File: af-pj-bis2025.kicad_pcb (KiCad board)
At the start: 2 copper layers, 70 x 88.8 mm, 101 parts, among them J1 Barrel_Jack_MountingPin, J10 Conn_01x02, J11 Conn_01x02, J2 CN7, J3 Conn_Coaxial, J4 Conn_Coaxial, J5 CN10, J6 Conn_01x10, J7 Conn_01x06, J8 Conn_01x02, J9 Conn_01x02, U1 MIC5237-5.0YU, U2 ALD114904APAL, U3 OPA2380AIDGKR, U4 THS4552IPWR, U5 REF5050IDR, U6 LT1991ACMS-TRPBF, U7 UA78L06ACPK, U8 ADS1220IPW

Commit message: initial commit
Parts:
- added D1: LED, LED_SMD:LED_0805_2012Metric_Pad1.15x1.40mm_HandSolder, F.Cu at (169.5, 70.0)
- added J12: FH28-10S-0.5SH_05_, pj-bis2025:HIROSE_FH28-10S-0.5SH_05_, F.Cu at (203.0, 139.0)
- added R32: 47, Resistor_SMD:R_0805_2012Metric_Pad1.20x1.40mm_HandSolder, F.Cu at (192.5, 130.0)
- added R33: 47, Resistor_SMD:R_0805_2012Metric_Pad1.20x1.40mm_HandSolder, F.Cu at (195.0, 130.0)
- added R34: 47, Resistor_SMD:R_0805_2012Metric_Pad1.20x1.40mm_HandSolder, F.Cu at (197.5, 130.0)
- added R35: 47, Resistor_SMD:R_0805_2012Metric_Pad1.20x1.40mm_HandSolder, F.Cu at (200.0, 130.0)
- added R36: 698, Resistor_SMD:R_0805_2012Metric_Pad1.20x1.40mm_HandSolder, F.Cu at (174.0, 70.0)
- added R37: 10k, Resistor_SMD:R_0805_2012Metric_Pad1.20x1.40mm_HandSolder, F.Cu at (168.5, 132.0)
- added SW1: PTS 647 SN50 SMTR2 LFS, pj-bis2025:PTS_647_SN50_SMTR2_LFS_PTS 647 SN50 SMTR2 LFS-M, F.Cu at (155.0, 76.5)
- added SW2: PTS 647 SN50 SMTR2 LFS, pj-bis2025:PTS_647_SN50_SMTR2_LFS_PTS 647 SN50 SMTR2 LFS-M, F.Cu at (161.0, 133.5)
- C1: footprint pj-bis2025:LDO_5V_out_TAJR105K016RNJAC_TAJR_AVX -> Capacitor_SMD:C_0805_2012Metric_Pad1.18x1.45mm_HandSolder
- C11, C9: value 3.18n -> 47n
- C12, C7: value 0.1u -> 47n
- C20, C6, C8: value 0.1u -> 0.1u_pass
- C4, C5: value 3.18n -> 4.7n
- R3, R4: value 50k -> 2.4k
- U1: value MIC5237-5.0YU -> MIC5237-5.0YT; footprint pj-bis2025:MIC5237-TO-263-3_MCL-M -> pj-bis2025:MIC5237_5_0YT
- moved J6 9.00 mm to (170.8, 139.0)
- moved TP10 8.49 mm to (159.5, 140.0)
- moved TP11 8.49 mm to (164.0, 140.0)
- moved TP8 8.49 mm to (150.5, 140.0)
- moved TP9 8.49 mm to (155.0, 140.0)
- moved U1 7.71 mm to (169.9, 78.0)
- moved C6 6.71 mm to (174.5, 128.8)
- moved C8 6.25 mm to (182.5, 128.8)
- moved TP5 1.80 mm to (150.0, 83.5)
- moved TP14 1.00 mm to (157.0, 83.5)
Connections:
- J2 pad 23: unconnected-(J2-Pin_23-Pad23) -> Net-(J2-Pin_23)
- J6 pad 10: /LCD_SCLK -> Net-(J6-Pin_10)
- J6 pad 7: /LCD_EXTCOMIN -> Net-(J6-Pin_7)
- J6 pad 8: /LCD_CS -> Net-(J6-Pin_8)
- J6 pad 9: /LCD_MOSI -> Net-(J6-Pin_9)
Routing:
- net GND: track 167.2 -> 225.0 mm, vias 3 -> 5
- net +3V3: track 83.6 -> 133.9 mm, vias 0 -> 2
- net /~{RST}: track 0.00 -> 35.6 mm, vias 0 -> 1
- net Net-(J6-Pin_8): track 0.00 -> 32.2 mm, vias 0 -> 2
- net Net-(J2-Pin_23): track 0.00 -> 30.0 mm
- net Net-(J6-Pin_7): track 0.00 -> 27.3 mm, vias 0 -> 2
- net Net-(J6-Pin_9): track 0.00 -> 27.3 mm, vias 0 -> 1
- net Net-(J6-Pin_10): track 0.00 -> 25.1 mm, vias 0 -> 1
- net /LCD_DISP: track 29.4 -> 44.1 mm, vias 0 -> 1
- net /DC_9V: track 41.1 -> 50.6 mm
- net /ADC_DRDY: track 62.0 -> 53.6 mm, vias 2 -> 1
- net /LCD_EXTCOMIN: track 29.5 -> 21.8 mm, vias 0 -> 1
- net /LCD_CS: track 40.5 -> 33.7 mm, vias 1 -> 0
- net /ADC_SCLK: track 66.3 -> 72.7 mm
- net /LCD_SCLK: track 38.7 -> 34.0 mm
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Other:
- board size 70 x 88.8 mm -> 70 x 93.2 mm
- board text added: "2026 Yusuke Akagi"
- board text removed: "2025 Yusuke Akagi"

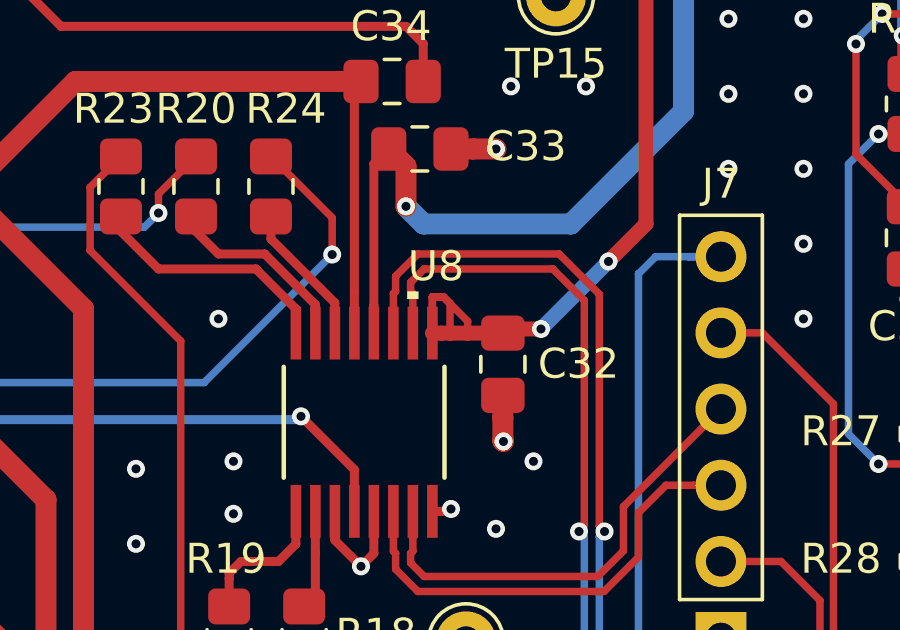
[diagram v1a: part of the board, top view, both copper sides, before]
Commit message: change PCB layout
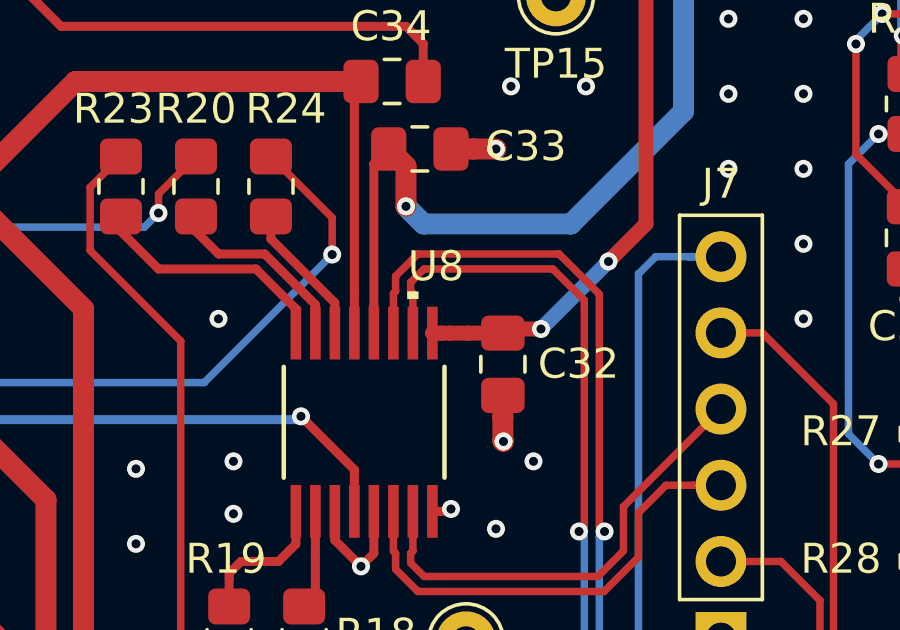
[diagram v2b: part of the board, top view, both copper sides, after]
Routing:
- net /VREF_5V: track 53.0 -> 47.0 mm
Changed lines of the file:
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@@
-	)
-	(segment
-		(start 168.468 109.738)
-		(end 168.247 109.518)
-		(width 0.25)
-		(layer "F.Cu")
-		(net 14)
 	)
 	(segment
@@
 		(end 171.397 88.816)
 		(width 0.5)
-		(layer "F.Cu")
-		(net 14)
-	)
-	(segment
-		(start 169.055 110.326)
-		(end 169.055 110.726)
-		(width 0.25)
 		(layer "F.Cu")
 		(net 14)
@@
 	)
 	(segment
-		(start 167.88 110.726)
-		(end 167.88 109.518)
-		(width 0.25)
-		(layer "F.Cu")
-		(net 14)
-	)
-	(segment
 		(start 170.2304 110.7261)
 		(end 170.2302 110.7259)
@@
 		(end 173.75 108.338)
 		(width 0.5)
-		(layer "F.Cu")
-		(net 14)
-	)
-	(segment
-		(start 168.468 110.726)
-		(end 168.468 109.738)
-		(width 0.25)
 		(layer "F.Cu")
 		(net 14)
@@
 	)
 	(segment
-		(start 167.88 110.726)
-		(end 167.88 109.518)
-		(width 0.25)
-		(layer "F.Cu")
-		(net 14)
-	)
-	(segment
 		(start 175 89.6819)
 		(end 175 91.1509)
@@
 	)
 	(segment
-		(start 167.88 109.518)
-		(end 168.248 109.518)
-		(width 0.25)
-		(layer "F.Cu")
-		(net 14)
-	)
-	(segment
-		(start 167.8805 110.726)
-		(end 167.8804 110.7261)
-		(width 0.25)
-		(layer "F.Cu")
-		(net 14)
-	)
-	(segment
 		(start 172.5 90.128)
 		(end 172.5 89.9185)
-		(width 0.25)
-		(layer "F.Cu")
-		(net 14)
-	)
-	(segment
-		(start 168.248 109.518)
-		(end 169.055 110.326)
 		(width 0.25)
 		(layer "F.Cu")
@@
 		(width 0.25)
 		(layer "F.Cu")
-		(net 14)
-	)
-	(segment
-		(start 168.247 109.518)
-		(end 167.88 109.518)
-		(width 0.25)
-		(layer "F.Cu")

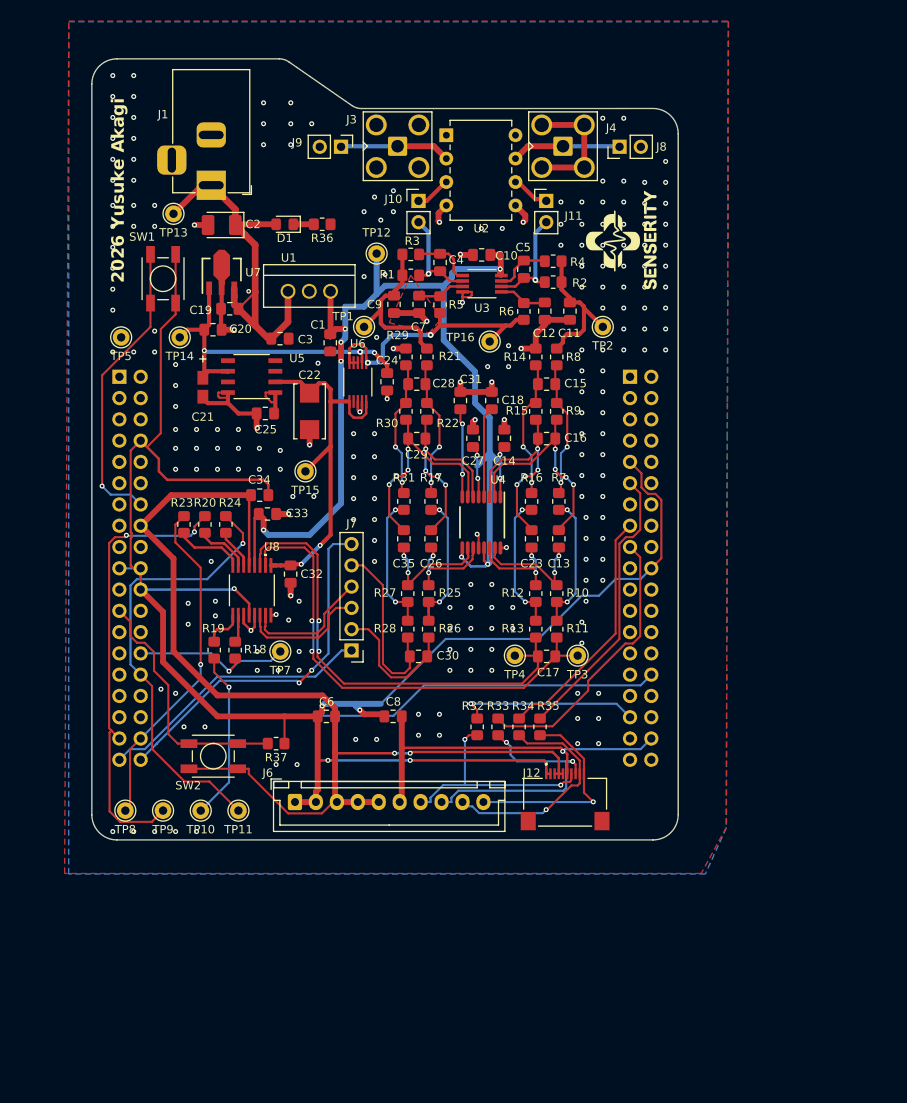
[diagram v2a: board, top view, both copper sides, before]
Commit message: 0.5Vrefのフットプリントを更新
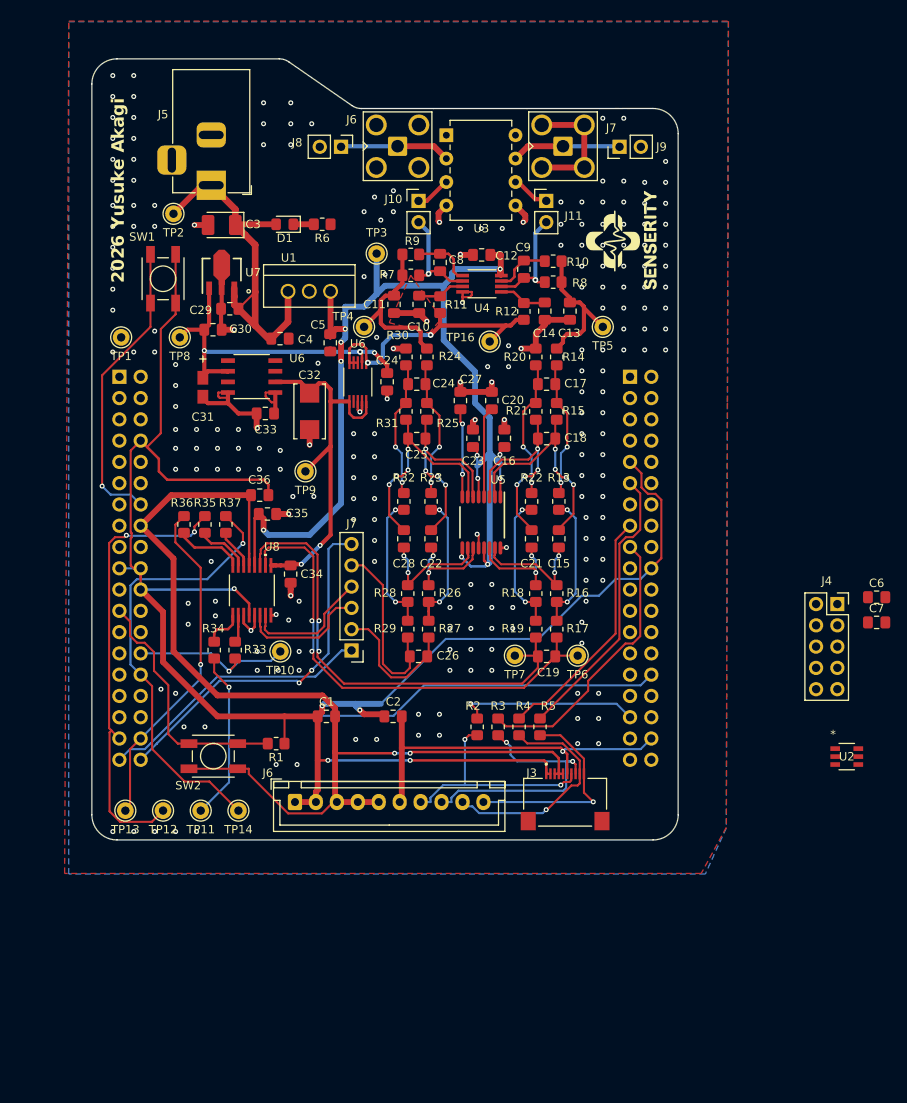
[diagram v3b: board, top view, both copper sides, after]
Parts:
- added C6: 0.1u, Capacitor_SMD:C_0805_2012Metric_Pad1.18x1.45mm_HandSolder, F.Cu at (240.2, 114.5)
- added C7: 0.1u, Capacitor_SMD:C_0805_2012Metric_Pad1.18x1.45mm_HandSolder, F.Cu at (240.2, 117.5)
- added J4: Conn_02x05_Odd_Even, Connector_PinSocket_2.54mm:PinSocket_2x05_P2.54mm_Vertical, F.Cu at (235.5, 115.3)
- added U2: ADR130BUJZ-REEL7, pj-bis2025:ADR130BUJZ_REEL7, F.Cu at (236.6, 133.5)
- renumbered C6 to C1, C7 to C10, C9 to C11, C10 to C12, C11 to C13, C12 to C14, C13 to C15, C14 to C16, C15 to C17, C16 to C18, C17 to C19, C8 to C2, C18 to C20, C23 to C21, C26 to C22, C27 to C23, C28 to C24, C29 to C25, C30 to C26, C31 to C27, C35 to C28, C19 to C29, C2 to C3, C20 to C30, C21 to C31, C22 to C32, C25 to C33, C32 to C34, C33 to C35, C34 to C36, C3 to C4, C1 to C5, C4 to C8, C5 to C9, J2 to J1, J5 to J2, J12 to J3, J1 to J5, J3 to J6, J4 to J7, J9 to J8, J8 to J9, R37 to R1, R4 to R10, R5 to R11, R6 to R12, R7 to R13, R8 to R14, R9 to R15, R10 to R16, R11 to R17, R12 to R18, R13 to R19, R32 to R2, R14 to R20, R15 to R21, R16 to R22, R17 to R23, R21 to R24, R22 to R25, R25 to R26, R26 to R27, R27 to R28, R28 to R29, R33 to R3, R29 to R30, R30 to R31, R31 to R32, R18 to R33, R19 to R34, R20 to R35, R23 to R36, R24 to R37, R34 to R4, R35 to R5, R36 to R6, R1 to R7, R2 to R8, R3 to R9, TP5 to TP1, TP7 to TP10, TP10 to TP11, TP9 to TP12, TP8 to TP13, TP11 to TP14, TP13 to TP2, TP12 to TP3, TP1 to TP4, TP2 to TP5, TP3 to TP6, TP4 to TP7, TP14 to TP8, TP15 to TP9, U2 to U3, U3 to U4, U4 to U5, U5 to U6
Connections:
- C26 pad 1: /AIN2_inP -> /AIN2P
- C26 pad 2: /AIN2_inN -> /AIN2N
- J3 pad 10: Net-(J6-Pin_10) -> Net-(J4-Pin_10)
- J3 pad 7: Net-(J6-Pin_7) -> Net-(J4-Pin_7)
- J3 pad 8: Net-(J6-Pin_8) -> Net-(J4-Pin_8)
- J3 pad 9: Net-(J6-Pin_9) -> Net-(J4-Pin_9)
- R2 pad 2: Net-(J6-Pin_7) -> Net-(J4-Pin_7)
- R27 pad 2: /AIN2_inN -> /AIN2N
- R29 pad 2: /AIN2_inP -> /AIN2P
- R3 pad 2: Net-(J6-Pin_8) -> Net-(J4-Pin_8)
- R4 pad 2: Net-(J6-Pin_9) -> Net-(J4-Pin_9)
- R5 pad 2: Net-(J6-Pin_10) -> Net-(J4-Pin_10)
- U8 pad 6: /AIN2_adcN -> /AIN2N
- U8 pad 7: /AIN2_adcP -> /AIN2P

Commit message: アナログ配線完了
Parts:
- removed the C24 at (181.8, 88.8)
- removed the J6 at (170.8, 139.0)
- removed the J7 at (177.5, 120.9)
- removed the U6 at (178.2, 88.8)
- added TP15: TestPoint, Connector_Pin:Pin_D1.0mm_L10.0mm, F.Cu at (187.0, 124.5)
- added TP16: TestPoint, Connector_Pin:Pin_D1.0mm_L10.0mm, F.Cu at (184.0, 124.5)
- C3: value C_Vin -> 22u
- C4: value 1µF -> 1u
- moved J4 108.1 mm to (141.3, 168.5), turned to 90 degrees
- moved U2 72.2 mm to (179.5, 89.4), turned to 90 degrees
- moved C7 69.1 mm to (178.9, 85.5), turned to 180 degrees
- moved C6 64.0 mm to (180.0, 93.0), turned to 180 degrees
- moved C1 48.0 mm to (142.5, 164.5)
- moved C2 48.0 mm to (150.4, 164.5)
- moved R36 44.7 mm to (189.5, 137.0), turned to 90 degrees
- moved J3 44.2 mm to (171.0, 169.5)
- moved R2 44.2 mm to (160.5, 160.5)
- moved R3 44.2 mm to (163.0, 160.5)
- moved R4 44.2 mm to (165.5, 160.5)
- moved R5 44.2 mm to (168.0, 160.5)
- moved R34 41.5 mm to (200.5, 134.0), turned to 180 degrees
- moved R35 41.2 mm to (187.0, 137.0), turned to -90 degrees
- moved R33 38.5 mm to (200.5, 132.0), turned to 180 degrees
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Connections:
- U8 pad 10: /AIN1N -> /AIN2N
- U8 pad 11: /AIN1P -> /AIN2P
- U8 pad 6: /AIN2N -> /AIN1N
- U8 pad 7: /AIN2P -> /AIN1P
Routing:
- net GND: track 225.0 -> 24.1 mm, vias 5 -> 0
- net +3V3: track 133.9 -> 10.7 mm, vias 2 -> 3
- net /ADC_SCLK: track 72.7 -> 0.00 mm, vias 1 -> 0
- net /ADC_MISO: track 54.2 -> 0.00 mm, vias 2 -> 0
- net /AIN1N: track 59.3 -> 13.5 mm, vias 2 -> 0
- net /AIN1P: track 57.0 -> 11.5 mm, vias 2 -> 0
- net /AIN2_mcuP: track 44.6 -> 0.00 mm, vias 2 -> 0
- net /LCD_DISP: track 44.1 -> 0.00 mm, vias 1 -> 0
- net GNDA: track 89.5 -> 52.2 mm, vias 227 -> 200
- net /LCD_SCLK: track 34.0 -> 0.00 mm
- net /LCD_CS: track 33.7 -> 0.00 mm
- net /AIN2_mcuN: track 33.4 -> 0.00 mm
- net Net-(J6-Pin_8): track 32.2 -> 0.00 mm, vias 2 -> 0
- net Net-(J4-Pin_8): track 0.00 -> 32.2 mm, vias 0 -> 2
- net /ADC_MOSI: track 40.6 -> 9.37 mm, vias 1 -> 0
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
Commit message: GND以外終わり
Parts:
- moved J4 68.8 mm to (161.1, 102.6), turned to 0 degrees
- moved C1 61.9 mm to (155.5, 104.0), turned to 90 degrees
- moved C2 56.3 mm to (155.5, 108.5), turned to -90 degrees
- moved TP11 49.1 mm to (208.5, 137.5)
- moved R2 48.2 mm to (170.1, 113.2), turned to 180 degrees
- moved J3 46.8 mm to (161.1, 123.8), turned to -90 degrees
- moved R3 45.3 mm to (170.1, 115.8), turned to 180 degrees
- moved R4 42.5 mm to (170.1, 118.2), turned to 180 degrees
- moved R5 39.8 mm to (170.1, 120.8), turned to 180 degrees
- moved SW1 32.4 mm to (167.0, 106.6)
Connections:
- J1 pad 1: unconnected-(J1-Pin_1-Pad1) -> /LCD_DISP
- J1 pad 2: unconnected-(J1-Pin_2-Pad2) -> /LCD_CS
- J1 pad 3: unconnected-(J1-Pin_3-Pad3) -> /LCD_EXTCOMIN
- J2 pad 15: /LCD_MOSI -> unconnected-(J2-Pin_15-Pad15)
- J2 pad 17: /LCD_CS -> unconnected-(J2-Pin_17-Pad17)
- J2 pad 29: unconnected-(J2-Pin_29-Pad29) -> /LCD_MOSI
- J2 pad 33: /LCD_EXTCOMIN -> unconnected-(J2-Pin_33-Pad33)
- J2 pad 36: /LCD_DISP -> unconnected-(J2-Pin_36-Pad36)
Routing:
- net /LCD_SCLK: track 0.00 -> 106.3 mm, vias 0 -> 3
- net /LCD_MOSI: track 0.00 -> 82.9 mm, vias 0 -> 3
- net +3V3: track 10.7 -> 93.4 mm, vias 3 -> 0
- net /ADC_CS: track 3.00 -> 78.9 mm
- net /ADC_MISO: track 0.00 -> 52.5 mm, vias 0 -> 2
- net /LCD_DISP: track 0.00 -> 50.6 mm, vias 0 -> 3
- net /LCD_CS: track 0.00 -> 42.8 mm
- net /ADC_MOSI: track 9.37 -> 51.7 mm
- net /LCD_EXTCOMIN: track 0.00 -> 39.0 mm
- net /ADC_SCLK: track 0.00 -> 27.5 mm
- net /ADC_DRDY: track 22.8 -> 44.1 mm
- net Net-(J4-Pin_10): track 25.1 -> 8.21 mm, vias 1 -> 0
- net /~{RST}: track 35.6 -> 21.8 mm, vias 1 -> 0
- net Net-(J4-Pin_8): track 32.2 -> 24.5 mm
- net Net-(J4-Pin_9): track 27.3 -> 20.3 mm, vias 1 -> 0
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
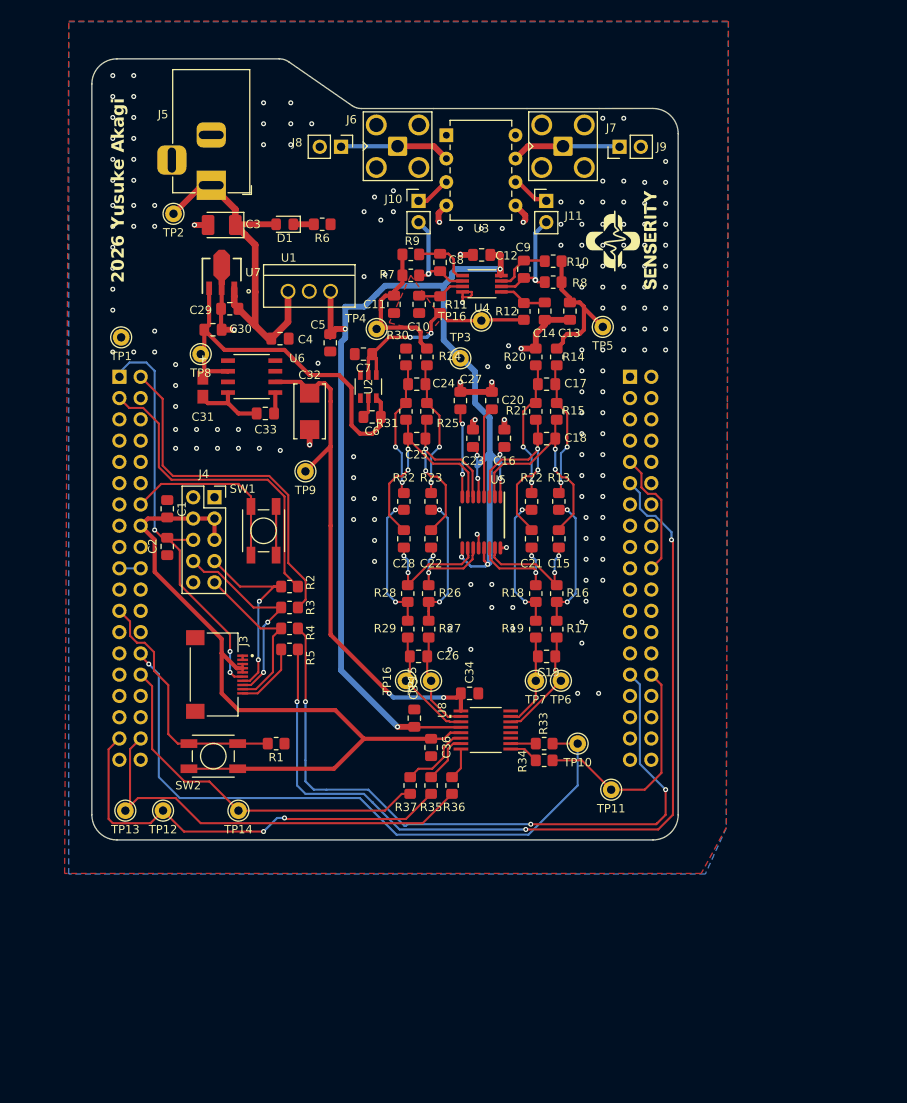
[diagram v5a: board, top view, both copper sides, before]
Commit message: GNDベタを配置
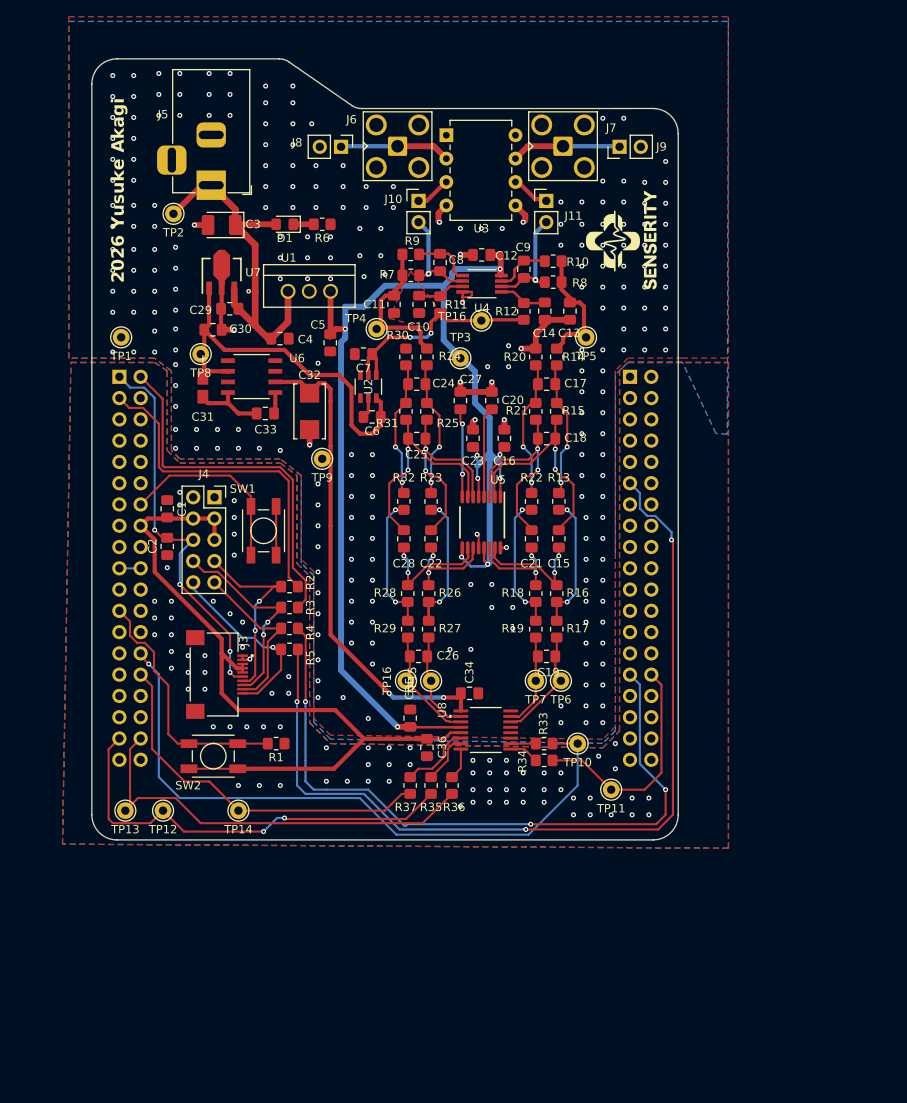
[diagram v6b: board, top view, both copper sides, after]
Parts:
- moved TP9 2.50 mm to (174.0, 98.0)
- moved TP5 2.36 mm to (205.5, 83.5)
- moved C35 0.50 mm to (184.5, 129.0)
- moved C36 0.50 mm to (186.5, 132.5)
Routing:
- net Net-(J4-Pin_10): track 8.21 -> 22.5 mm, vias 0 -> 1
- net GND: track 24.1 -> 10.1 mm, vias 0 -> 79
- net /VREF_5V: track 62.7 -> 58.5 mm
- net /LCD_DISP: track 50.6 -> 47.3 mm, vias 3 -> 4
- net /OUT1: track 17.6 -> 14.4 mm
- net /LCD_CS: track 42.8 -> 44.2 mm
- net /LCD_EXTCOMIN: track 39.0 -> 40.4 mm
- net /~{RST}: track 21.8 -> 22.6 mm
- net GNDA: vias 163 -> 252
- net /AVDD_6.2V: vias 1 -> 0
- net /ADC_SCLK: vias 0 -> 2
- added copper zone on B.Cu, net GND
- added copper zone on F.Cu, net GND

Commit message: savd
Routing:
- net GNDA: track 52.2 -> 70.2 mm, vias 252 -> 259
- net GND: track 10.1 -> 27.6 mm, vias 79 -> 96
- net /ADC_SCLK: track 27.5 -> 25.9 mm, vias 2 -> 0

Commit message: save
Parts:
- removed the TP16 at (193.0, 81.5)
- added TP17: TestPoint, Connector_Pin:Pin_D1.0mm_L10.0mm, F.Cu at (193.0, 81.5)
